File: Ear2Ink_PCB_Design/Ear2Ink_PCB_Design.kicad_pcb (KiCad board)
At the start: 2 copper layers, 63.5 x 69.8 mm, 67 parts, among them J1 Conn_01x16_Pin, J2 Conn_01x08_Pin, J3 Conn_01x08_Pin, J4 MEM2052-00-195-00-A_REVA, J5 Conn_01x06_Pin, J6 Conn_01x04_Pin, J7 Conn_01x03_Pin, J8 Conn_01x16_Pin, P1 OSTTE020104, SW1 SW_Push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

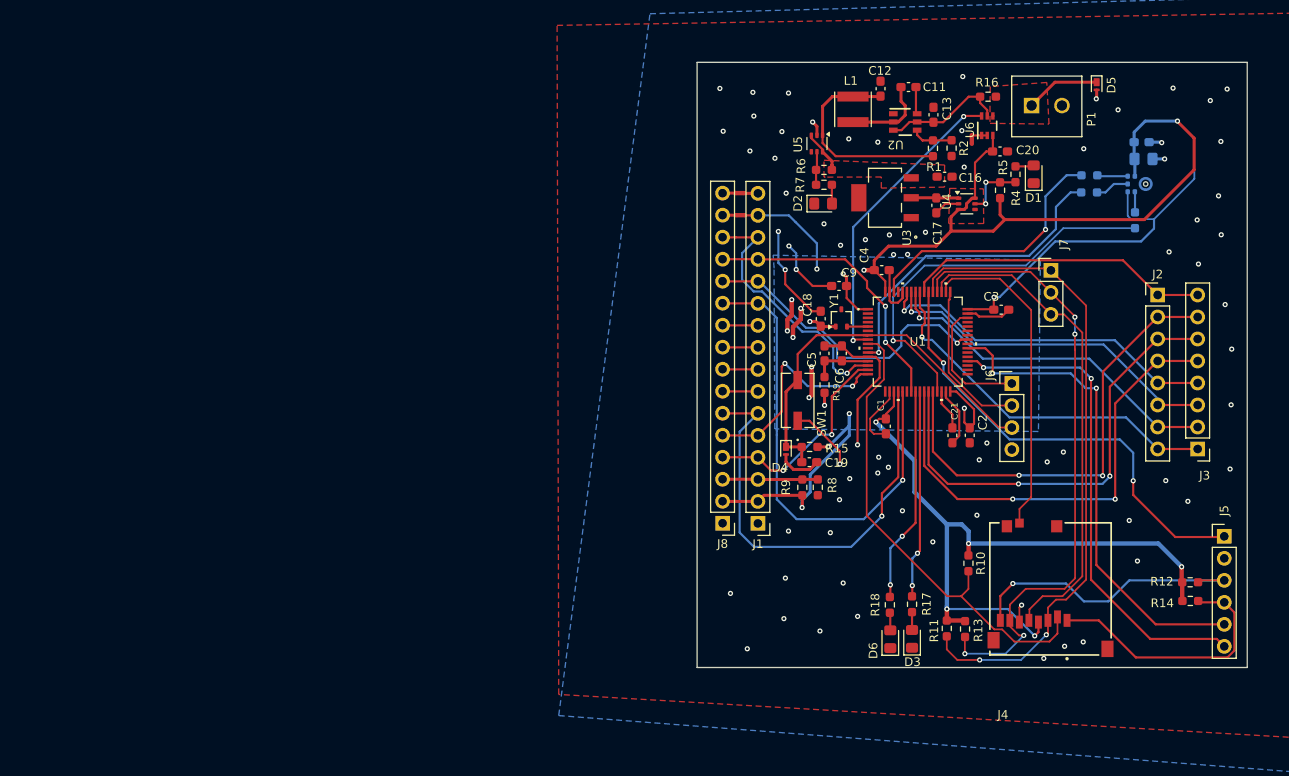
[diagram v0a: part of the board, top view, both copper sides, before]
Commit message: New Parts Added
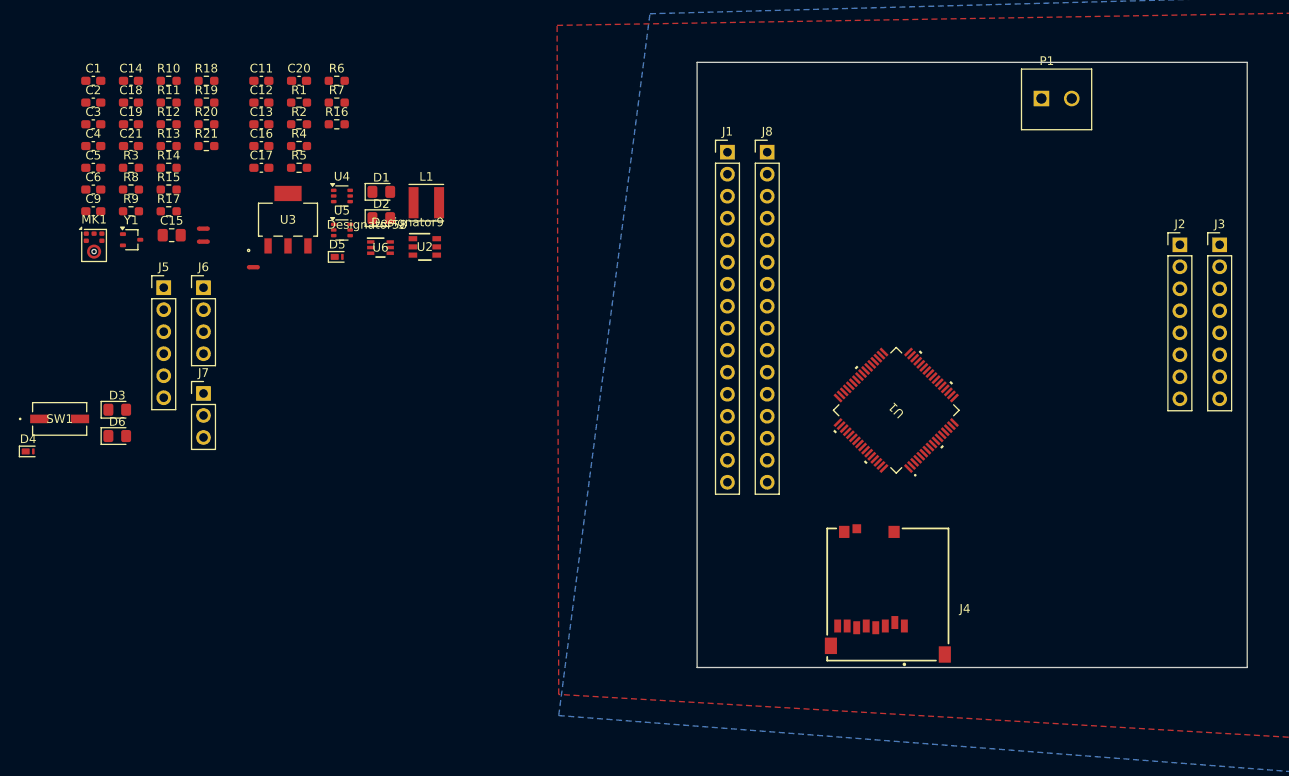
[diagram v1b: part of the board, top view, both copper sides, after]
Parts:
- C14, C15, MK1, R20, R21, R3: moved to F.Cu
- L1: value IFSC1515AHER4R7M01 -> 47uH
- R17, R18, R5: value 330 -> 220
- moved R12 129.2 mm to (61.5, 38.1)
- moved R14 128.1 mm to (61.5, 43.1)
- moved J5 125.7 mm to (61.0, 57.0)
- moved MK1 120.9 mm to (52.9, 52.1), turned to 0 degrees
- moved C14 116.9 mm to (57.2, 33.1)
- moved C15 112.5 mm to (61.9, 50.9)
- moved R3 110.6 mm to (57.2, 43.1)
- moved R11 108.4 mm to (61.5, 35.6), turned to 0 degrees
- moved C2 108.2 mm to (52.8, 35.6), turned to 0 degrees
- moved R10 107.8 mm to (61.5, 33.1), turned to 0 degrees
- moved R20 107.8 mm to (65.9, 38.1), turned to 0 degrees
- moved R13 107.5 mm to (61.5, 40.6), turned to 0 degrees
- moved C3 107.0 mm to (52.8, 38.1)
- moved R21 102.0 mm to (65.9, 40.6)
- moved C21 100.5 mm to (57.2, 40.6), turned to 0 degrees
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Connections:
- U3 pad 4: GND -> (no net)
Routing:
- net +3.3V: track 282.5 -> 0.00 mm, vias 22 -> 0
- net GND: track 88.4 -> 0.00 mm, vias 75 -> 0
- net SPI3_MOSI: track 76.7 -> 0.00 mm, vias 2 -> 0
- net SPI3_MISO: track 73.0 -> 0.00 mm, vias 4 -> 0
- net SPI3_SCK: track 57.5 -> 0.00 mm
- net SDIO_CK: track 56.9 -> 0.00 mm, vias 2 -> 0
- net SDIO_D0: track 56.0 -> 0.00 mm, vias 2 -> 0
- net CS: track 55.6 -> 0.00 mm
- net DB4: track 55.5 -> 0.00 mm, vias 1 -> 0
- net C4: track 54.8 -> 0.00 mm, vias 2 -> 0
- net C3: track 53.4 -> 0.00 mm, vias 2 -> 0
- net C2: track 53.3 -> 0.00 mm, vias 2 -> 0
- net SDIO_CMD: track 53.2 -> 0.00 mm, vias 2 -> 0
- net EN: track 52.5 -> 0.00 mm, vias 1 -> 0
- net NRST: track 45.3 -> 0.00 mm
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- removed copper zone on B.Cu, net +3.3V
- removed copper zone on F.Cu, net +3.3V
- removed copper zone on F.Cu, net 5V
- removed copper zone on F.Cu, net 9V

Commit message: Did a lot of stuff
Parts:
- removed J7: Conn_01x03_Pin, Connector_PinHeader_2.54mm:PinHeader_1x03_P2.54mm_Vertical
- added FB1: 600, Resistor_SMD:R_0603_1608Metric_Pad0.98x0.95mm_HandSolder, F.Cu at (156.3, 73.7)
- added JP1: SolderJumper_2_Open, Jumper:SolderJumper-2_P1.3mm_Open_Pad1.0x1.5mm, F.Cu at (170.9, 44.3)
- added R22: 10k, Resistor_SMD:R_0603_1608Metric_Pad0.98x0.95mm_HandSolder, B.Cu at (140.1, 78.9)
- C14, C15, MK1, NT1, R20, R21, R3: moved to B.Cu
- R19: value 10 -> 1M
- moved NT2 151.1 mm to (214.9, 73.3)
- moved NT3 151.1 mm to (214.9, 74.8)
- moved C16 151.1 mm to (221.6, 63.8)
- moved C21 151.1 mm to (206.5, 63.8)
- moved C5 151.1 mm to (202.2, 66.3)
- moved C6 151.1 mm to (202.2, 68.8)
- moved R6 151.1 mm to (230.3, 56.3)
- moved R7 151.1 mm to (230.3, 58.8)
- moved R8 151.1 mm to (206.5, 68.8)
- moved R9 151.1 mm to (206.5, 71.3)
- moved R10 146.2 mm to (205.8, 57.0)
- moved D4 117.1 mm to (162.4, 76.6), turned to -90 degrees
- moved SW1 116.9 mm to (165.7, 78.9), turned to 90 degrees
- moved C19 109.0 mm to (158.9, 77.2), turned to -90 degrees
- moved R19 108.9 mm to (154.6, 98.7)
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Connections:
- net Net-(U2-EN) renamed /Power Conversions + Battery Monitor/Buck_In
- net Net-(U3-VO) renamed /Power Conversions + Battery Monitor/LDO_Out
- net Net-(U5-VIN) renamed /Power Conversions + Battery Monitor/5V_Out
- J4 pad G1: GND -> Net-(J4-SHIELD_GND)
- J4 pad G2: GND -> Net-(J4-SHIELD_GND)
- J4 pad G3: GND -> Net-(J4-SHIELD_GND)
- J4 pad G4: GND -> Net-(J4-SHIELD_GND)
- J5 pad 1: SDIO_CMD -> GND
- J5 pad 2: GND -> SD_DAT2
- J5 pad 4: SD_DAT2 -> SDIO_CMD
- R19 pad 1: +3.3V -> Net-(J4-SHIELD_GND)
- R19 pad 2: +3.3VA -> GND
- U1 pad 60: GND -> Net-(U1-BOOT0)
- U6 pad 2: GNDA -> GND
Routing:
- net +3.3V: track 0.00 -> 59.0 mm, vias 0 -> 7
- net GNDA: track 0.00 -> 36.8 mm, vias 0 -> 1
- net SYS_SWCLK: track 0.00 -> 32.5 mm
- net SYS_SWDIO: track 0.00 -> 31.5 mm
- net R2: track 0.00 -> 30.2 mm, vias 0 -> 1
- net SPI3_MOSI: track 0.00 -> 30.1 mm, vias 0 -> 1
- net GND: track 0.00 -> 28.7 mm, vias 0 -> 19
- net SPI3_MISO: track 0.00 -> 27.8 mm, vias 0 -> 3
- net SPI3_SCK: track 0.00 -> 26.0 mm, vias 0 -> 1
- net SD_DAT2: track 0.00 -> 24.2 mm, vias 0 -> 1
- net /Power Conversions + Battery Monitor/5V_Out: track 0.00 -> 21.7 mm
- net NRST: track 0.00 -> 21.3 mm
- net I2S2_SD: track 0.00 -> 21.0 mm, vias 0 -> 1
- net R4: track 0.00 -> 20.1 mm, vias 0 -> 1
- net I2S2_WS: track 0.00 -> 19.5 mm, vias 0 -> 1
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- added copper zone on F.Cu, net +3.3V
- added copper zone on F.Cu, net /Power Conversions + Battery Monitor/5V_Out
- added copper zone on F.Cu, net /Power Conversions + Battery Monitor/Buck_In
- added copper zone on F.Cu, net /Power Conversions + Battery Monitor/LDO_Out
- added copper zone on F.Cu, net 9V
- added copper zone on F.Cu, net Net-(J4-SHIELD_GND)
- added copper zone on B.Cu, net Net-(U2-SW)
- added copper zone on F.Cu, net Net-(U2-SW)

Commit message: put everything on not done tho
almost done
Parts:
- NT1: moved to F.Cu
- moved NT3 86.7 mm to (128.2, 79.4), turned to 180 degrees
- moved NT2 86.6 mm to (128.3, 76.8), turned to 180 degrees
- moved R7 82.2 mm to (149.8, 42.5), turned to 180 degrees
- moved R6 82.0 mm to (149.8, 40.7)
- moved C16 80.2 mm to (145.5, 38.4), turned to 90 degrees
- moved R8 76.5 mm to (133.8, 45.3), turned to 90 degrees
- moved R9 76.4 mm to (135.4, 43.4), turned to 90 degrees
- moved R10 61.8 mm to (154.7, 91.8), turned to 180 degrees
- moved C21 56.0 mm to (150.6, 62.0), turned to 135 degrees
- moved C5 47.4 mm to (155.2, 73.2), turned to 90 degrees
- moved C6 45.4 mm to (157.0, 73.2), turned to 90 degrees
- moved D2 15.9 mm to (151.4, 44.5), turned to 180 degrees
- moved U5 3.07 mm to (149.1, 37.2), turned to -90 degrees
- moved FB1 2.56 mm to (158.8, 73.2), turned to -90 degrees
- moved D1 1.15 mm to (136.8, 50.5)
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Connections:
- U3 pad 4: (no net) -> /Power Conversions + Battery Monitor/LDO_Out
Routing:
- net CS: track 0.00 -> 32.0 mm
- net GND: track 28.7 -> 37.6 mm, vias 19 -> 51
- net Net-(U5-ST): track 0.00 -> 6.90 mm
- net +3.3V: track 59.0 -> 52.6 mm, vias 7 -> 5
- net Vee: track 4.89 -> 10.5 mm
- net Net-(U1-VCAP1): track 0.00 -> 4.53 mm
- net Net-(D2-A): track 0.00 -> 3.22 mm
- net +3.3VA: track 4.84 -> 7.98 mm
- net GNDA: track 36.8 -> 34.6 mm, vias 1 -> 0
- net LED-: track 0.00 -> 1.92 mm
- net LED+: track 0.00 -> 1.88 mm
- net SYS_SWDIO: track 31.5 -> 32.9 mm, vias 0 -> 1
- net I2S2_SD: track 21.0 -> 20.3 mm
- net SYS_SWCLK: track 32.5 -> 32.7 mm, vias 0 -> 1
- added copper zone on F.Cu, net 5V

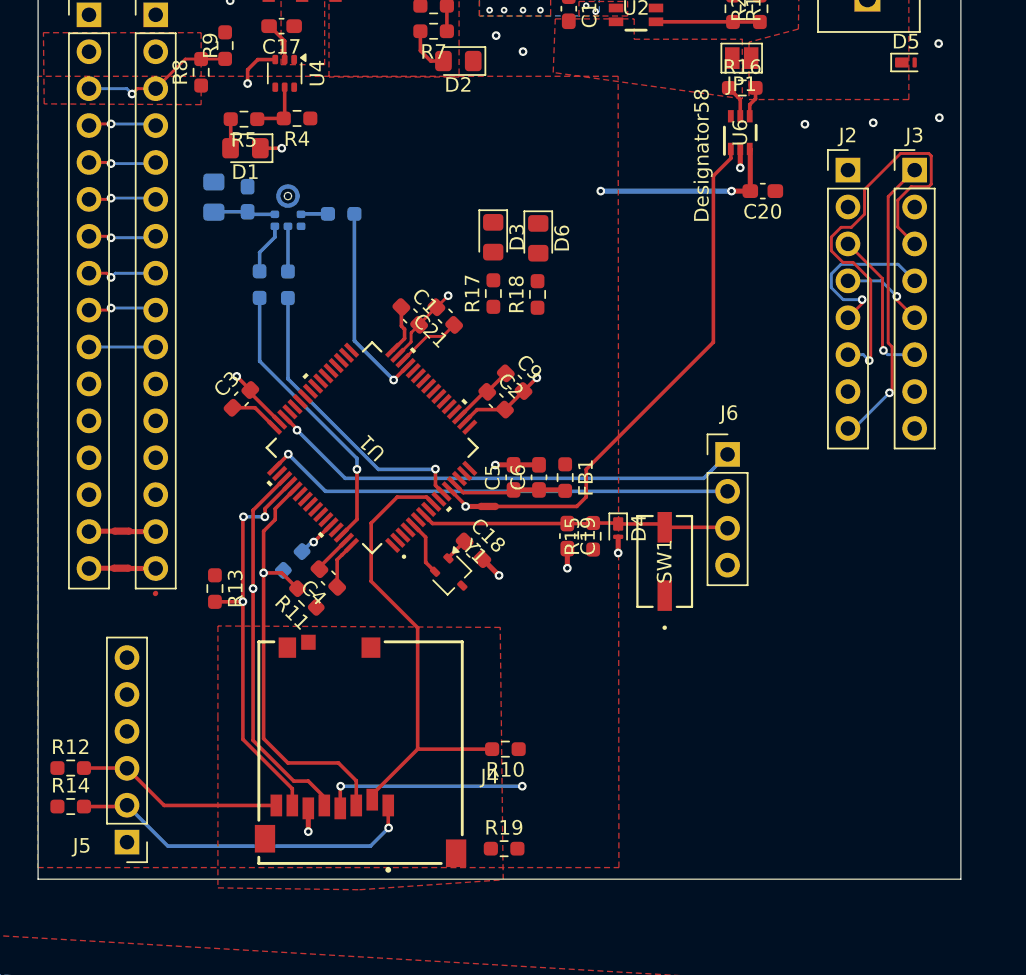
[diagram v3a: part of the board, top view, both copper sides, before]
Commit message: working through DRC, routing done
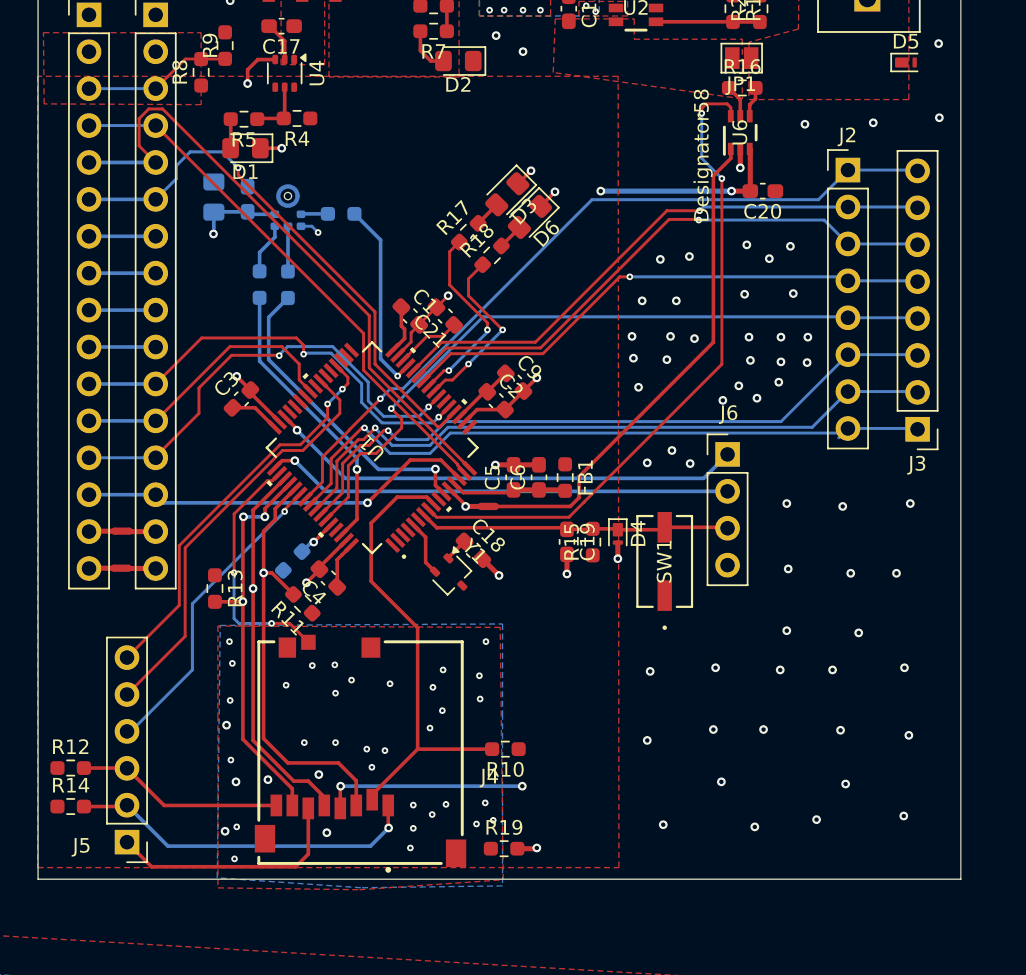
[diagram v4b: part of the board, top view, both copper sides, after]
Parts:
- moved J3 17.8 mm to (183.1, 69.8), turned to 180 degrees
- moved R17 4.52 mm to (152.2, 56.3), turned to 45 degrees
- moved R18 4.13 mm to (153.8, 57.9), turned to 45 degrees
- moved D3 3.11 mm to (154.8, 53.7), turned to -135 degrees
- moved D6 1.58 mm to (156.4, 55.2), turned to -135 degrees
- moved R11 0.49 mm to (140.8, 81.8)
- moved C19 0.40 mm to (158.9, 77.6)
- moved R15 0.40 mm to (160.7, 77.6)
- moved D4 0.40 mm to (162.4, 77.0)
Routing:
- net C1: track 0.00 -> 52.6 mm, vias 0 -> 1
- net R3: track 0.00 -> 46.9 mm, vias 0 -> 1
- net ADC10: track 0.00 -> 45.8 mm, vias 0 -> 2
- net C2: track 0.00 -> 39.4 mm, vias 0 -> 1
- net R/W: track 4.65 -> 43.6 mm, vias 1 -> 0
- net R1: track 11.5 -> 49.6 mm
- net EN: track 4.66 -> 37.8 mm
- net RS: track 4.68 -> 37.7 mm, vias 1 -> 0
- net DB6: track 0.00 -> 31.7 mm, vias 0 -> 2
- net C4: track 5.78 -> 37.1 mm
- net DB4: track 0.00 -> 30.2 mm, vias 0 -> 2
- net SDIO_D0: track 0.00 -> 29.0 mm
- net C3: track 10.6 -> 39.5 mm
- net SDIO_CK: track 0.00 -> 27.5 mm, vias 0 -> 2
- net DB7: track 0.00 -> 27.5 mm, vias 0 -> 1
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- added copper zone on B.Cu, net Net-(J4-SHIELD_GND)

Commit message: finshed routing and minimal drc
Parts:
- moved R10 0.35 mm to (154.7, 91.5)
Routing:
- net GND: track 58.0 -> 84.4 mm, vias 106 -> 114
- net Net-(J4-SHIELD_GND): track 0.00 -> 9.84 mm, vias 38 -> 6
- net 5V: track 0.00 -> 5.29 mm
- net /Power Conversions + Battery Monitor/Buck_In: track 2.27 -> 5.41 mm
- net Net-(U5-ST): track 6.90 -> 8.62 mm
- net SDIO_D0: track 29.0 -> 29.8 mm, vias 0 -> 2
- net SDIO_CK: vias 2 -> 0
- net Net-(U2-SW): vias 7 -> 6
- net +3.3V: vias 7 -> 29
- added copper zone on B.Cu, net +3.3V
- removed copper zone on B.Cu, net Net-(J4-SHIELD_GND)

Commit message: done
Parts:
- removed D1: LED, LED_SMD:LED_0805_2012Metric_Pad1.15x1.40mm_HandSolder
- removed D5: PTVS5V0Z1USK, Diode_SMD:Nexperia_DSN1608-2_1.6x0.8mm
- removed R4: 10k, Resistor_SMD:R_0603_1608Metric_Pad0.98x0.95mm_HandSolder
- removed R5: 220, Resistor_SMD:R_0603_1608Metric_Pad0.98x0.95mm_HandSolder
- removed U4: LM66100DCK, Package_TO_SOT_SMD:SOT-363_SC-70-6
- added C7: .1uF, Capacitor_SMD:C_0603_1608Metric_Pad1.08x0.95mm_HandSolder, F.Cu at (181.9, 38.2)
- added D10: PTVS5V0Z1USK, Diode_SMD:Nexperia_DSN1608-2_1.6x0.8mm, B.Cu at (178.7, 55.6)
- added D11: PTVS5V0Z1USK, Diode_SMD:Nexperia_DSN1608-2_1.6x0.8mm, B.Cu at (176.9, 57.3)
- added D12: PTVS5V0Z1USK, Diode_SMD:Nexperia_DSN1608-2_1.6x0.8mm, B.Cu at (178.1, 61.6)
- added D13: PTVS5V0Z1USK, Diode_SMD:Nexperia_DSN1608-2_1.6x0.8mm, B.Cu at (179.0, 64.2)
- added D14: PTVS5V0Z1USK, Diode_SMD:Nexperia_DSN1608-2_1.6x0.8mm, B.Cu at (180.0, 67.5)
- added D15: LED, LED_SMD:LED_0805_2012Metric_Pad1.15x1.40mm_HandSolder, F.Cu at (186.0, 40.1)
- added D16: LED, LED_SMD:LED_0805_2012Metric_Pad1.15x1.40mm_HandSolder, F.Cu at (153.1, 28.4)
- added D17: LED, LED_SMD:LED_0805_2012Metric_Pad1.15x1.40mm_HandSolder, F.Cu at (133.5, 41.2)
- added D7: PTVS5V0Z1USK, Diode_SMD:Nexperia_DSN1608-2_1.6x0.8mm, B.Cu at (177.6, 44.5)
- added D8: PTVS5V0Z1USK, Diode_SMD:Nexperia_DSN1608-2_1.6x0.8mm, B.Cu at (178.5, 47.0)
- added D9: PTVS5V0Z1USK, Diode_SMD:Nexperia_DSN1608-2_1.6x0.8mm, B.Cu at (179.4, 49.4)
- added G***: LOGO, LOGO, F.Cu at (108.5, 32.6)
- added H1: MountingHole, MountingHole:MountingHole_2.5mm, F.Cu at (185.4, 25.4)
- added H2: MountingHole, MountingHole:MountingHole_2.5mm, F.Cu at (88.9, 25.4)
- added H3: MountingHole, MountingHole:MountingHole_2.5mm, F.Cu at (87.1, 97.7)
- added H4: MountingHole, MountingHole:MountingHole_2.5mm, F.Cu at (185.4, 95.2)
- added R23: 690, Resistor_SMD:R_0603_1608Metric_Pad0.98x0.95mm_HandSolder, F.Cu at (181.9, 40.0)
- added R24: 330, Resistor_SMD:R_0603_1608Metric_Pad0.98x0.95mm_HandSolder, F.Cu at (153.1, 32.6)
- added R25: 120, Resistor_SMD:R_0603_1608Metric_Pad0.98x0.95mm_HandSolder, F.Cu at (133.5, 45.3)
- moved NT2 41.7 mm to (88.6, 89.7)
- moved J1 41.7 mm to (86.3, 54.2)
- moved J8 41.7 mm to (90.9, 54.2)
- moved NT3 41.7 mm to (88.6, 92.2)
- moved R9 37.1 mm to (100.6, 56.2)
- moved R8 36.9 mm to (98.5, 56.2), turned to -90 degrees
- moved U3 10.2 mm to (141.2, 46.8), turned to 90 degrees
- moved C17 9.61 mm to (146.8, 48.2), turned to -90 degrees
- moved J2 8.27 mm to (182.1, 44.7)
- moved J3 8.27 mm to (186.9, 62.5)
- moved P1 5.72 mm to (178.7, 32.8)
- moved R19 1.81 mm to (154.7, 96.9)
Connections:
- C17 pad 1: /Power Conversions + Battery Monitor/LDO_Out -> +3.3V
- J1 pad 15: +3.3V -> 5V
- J1 pad 2: +3.3V -> 5V
- J8 pad 2: +3.3V -> 5V
- NT2 pad 2: +3.3V -> 5V
- R8 pad 1: +3.3V -> 5V
- U3 pad 2: /Power Conversions + Battery Monitor/LDO_Out -> +3.3V
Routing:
- net 5V: track 5.29 -> 107.4 mm
- net DB4: track 30.4 -> 75.4 mm
- net DB5: track 19.3 -> 64.3 mm
- net DB7: track 27.5 -> 72.1 mm
- net DB6: track 31.7 -> 75.7 mm
- net EN: track 37.8 -> 76.7 mm
- net R/W: track 43.6 -> 78.4 mm
- net RS: track 37.7 -> 72.0 mm
- net C1: track 52.5 -> 64.0 mm
- net C2: track 39.4 -> 49.6 mm
- net GND: track 84.4 -> 75.7 mm, vias 114 -> 183
- net R3: track 46.8 -> 55.4 mm
- net R4: track 47.3 -> 55.6 mm
- net R2: track 47.3 -> 55.4 mm
- net C4: track 37.1 -> 44.8 mm
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- removed copper zone on F.Cu, net /Power Conversions + Battery Monitor/LDO_Out
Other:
- board size 63.5 x 69.8 mm -> 108 x 82.5 mm
- board text added: "Team 25's Awesome PCB Keona Fielitz, Dana Shi, Josh Wu, Aditi Akella"

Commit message: updated 5V resistor values
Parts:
- R1: value 60k -> 54.9k
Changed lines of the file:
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@@
 			)
 		)
-		(property "Value" "60k"
+		(property "Value" "54.9k"
 			(at 0 1.43 90)
 			(layer "F.Fab")
